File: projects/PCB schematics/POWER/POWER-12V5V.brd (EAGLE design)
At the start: 99.1 x 99.1 mm, 23 parts, among them U1 UCC383TDKTTT-5, U2 UCC383TDKTTT-5, U3 UCC383TDKTTT-5, X1 5566-2, X2 5566-2, X3 5566-2, X4 5566-2, X5 5566-2

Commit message: POWER - 12V5V revisions.
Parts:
- added X11, X6, X7, X9: 5566-2, con-molex:5566-2
- moved X1 16.5 mm to (52.1, 92.7)
- moved X5 8.89 mm to (43.2, 7.62)
- moved X3 7.62 mm to (15.2, 7.62)
- moved X4 6.35 mm to (85.1, 7.62)
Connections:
- net +12V-ISO: now also X6.1, X6.2
- net +5V: now also X9.1, X9.2
- net GND: now also X11.1, X11.2
- net VCC: now also X7.1, X7.2
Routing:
- added copper zone on layer 1, net +12V-ISO
- added copper zone on layer 1, net +5V
- added copper zone on layer 16, net GND

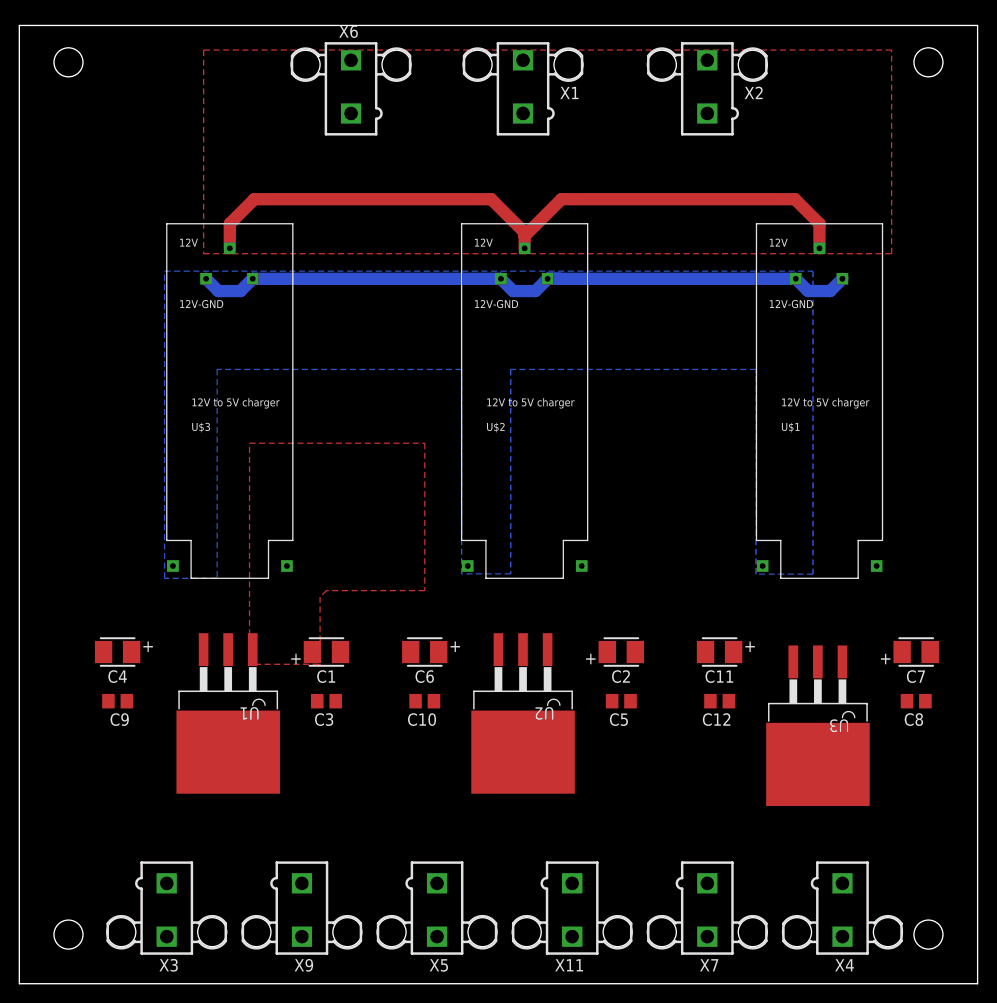
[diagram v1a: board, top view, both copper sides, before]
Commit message: AMAR - 12V5V initial routing.
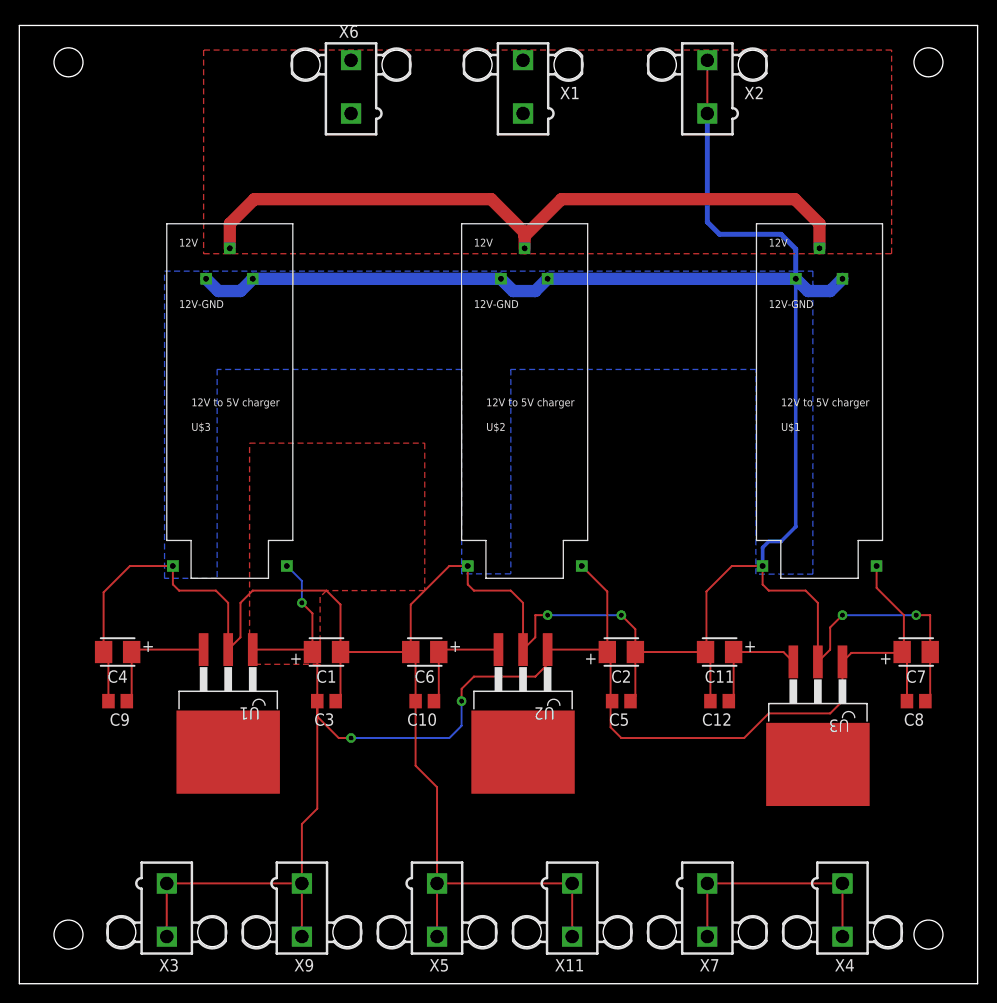
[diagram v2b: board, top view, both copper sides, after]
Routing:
- net GND: track 70.2 -> 361.0 mm, vias 0 -> 4
- net +5V: track 0.00 -> 175.9 mm, vias 0 -> 3
- net VCC: track 0.00 -> 25.0 mm
- net N$1: track 0.00 -> 12.8 mm
- net N$2: track 0.00 -> 11.9 mm
- net N$3: track 0.00 -> 11.6 mm

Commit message: POWER - 12V5V Rev A.
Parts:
- added C13, C14, C15: 100n, rcl:C0805
- C10, C12, C9: value (none) -> 1u
- renumbered X1 to +12V-ISO.2, X11 to GND.3, X2 to GND.1, X3 to +5V.2, X4 to VCC.1, X5 to GND.2, X6 to +12V-ISO.1, X7 to VCC.2, X9 to +5V.1
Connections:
- removed net N$1: C4.1, C9.1, U1.3
- removed net N$2: C11.1, C12.1, U3.3
- removed net N$3: C10.1, C6.1, U2.3
- net GND: now also C13.2, C14.2, C15.2
- net VCC: now also C10.1, C11.1, C12.1, C13.1, C14.1, C15.1, C4.1, C6.1, C9.1, U1.3, U2.3, U3.3
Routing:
- net GND: track 361.0 -> 232.8 mm, vias 4 -> 6
- net +5V: track 175.9 -> 54.7 mm, vias 3 -> 0
- net VCC: track 25.0 -> 61.5 mm, vias 0 -> 14
- net N$1: track 12.8 -> 0.00 mm
- net N$2: track 11.9 -> 0.00 mm
- net N$3: track 11.6 -> 0.00 mm
- added copper zone on layer 1, net GND
- added copper zone on layer 1, net VCC
- added copper zone on layer 16, net VCC
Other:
- board text added: "12VDC-5VDC Converter board (POWER-12V5V) Rev A: April 8th, 2019"
- board text added: "Authors: github.com/michaelpass github.com/AMarijo"
- board text added: "Iowa Formula"
